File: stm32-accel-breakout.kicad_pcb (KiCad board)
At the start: 2 copper layers, 43.1 x 38 mm, 42 parts, among them J1 USB_C_Receptacle_USB2.0, J2 JST-PH-01x05, J3 Conn_01x03, J5 Conn_01x04, U1 STM32F103C8Tx, U2 AP2112K-3.3, U3 ADXL335, Y1 Crystal_GND24

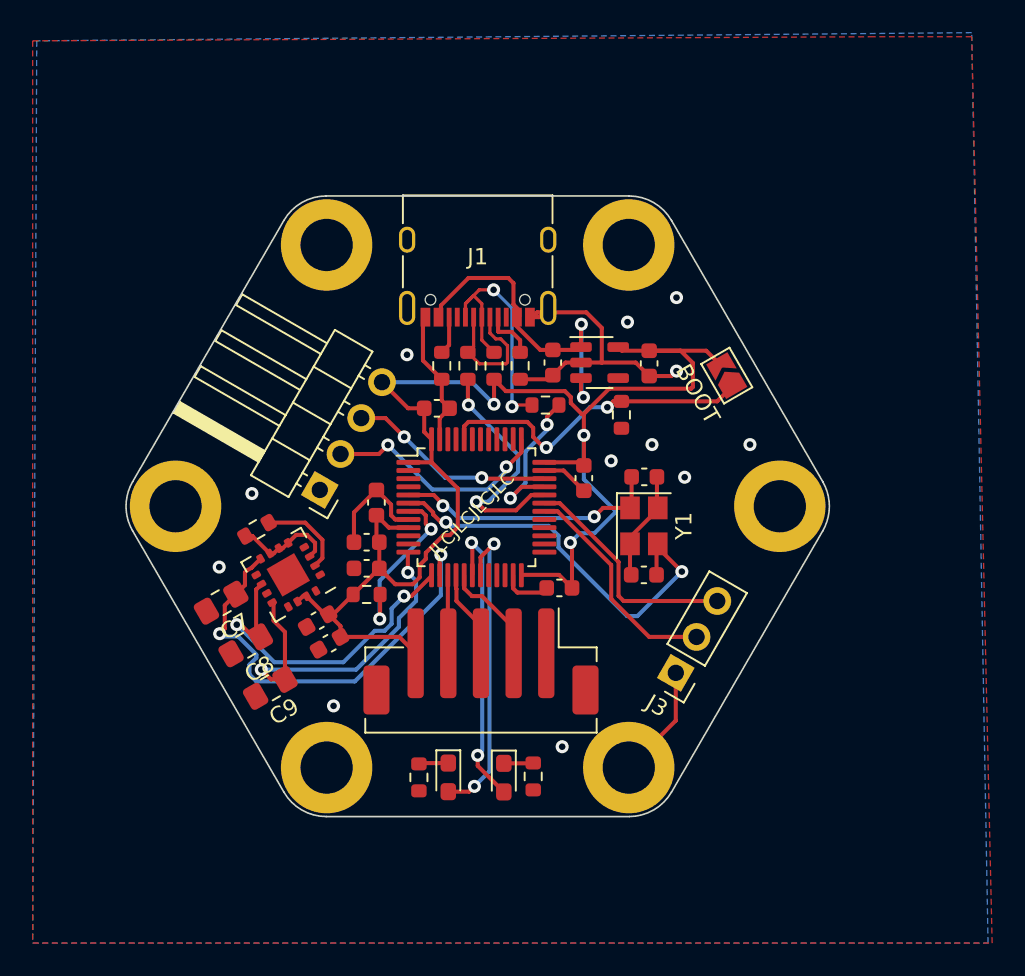
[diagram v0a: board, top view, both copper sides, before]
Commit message: changed programming header to tag connect
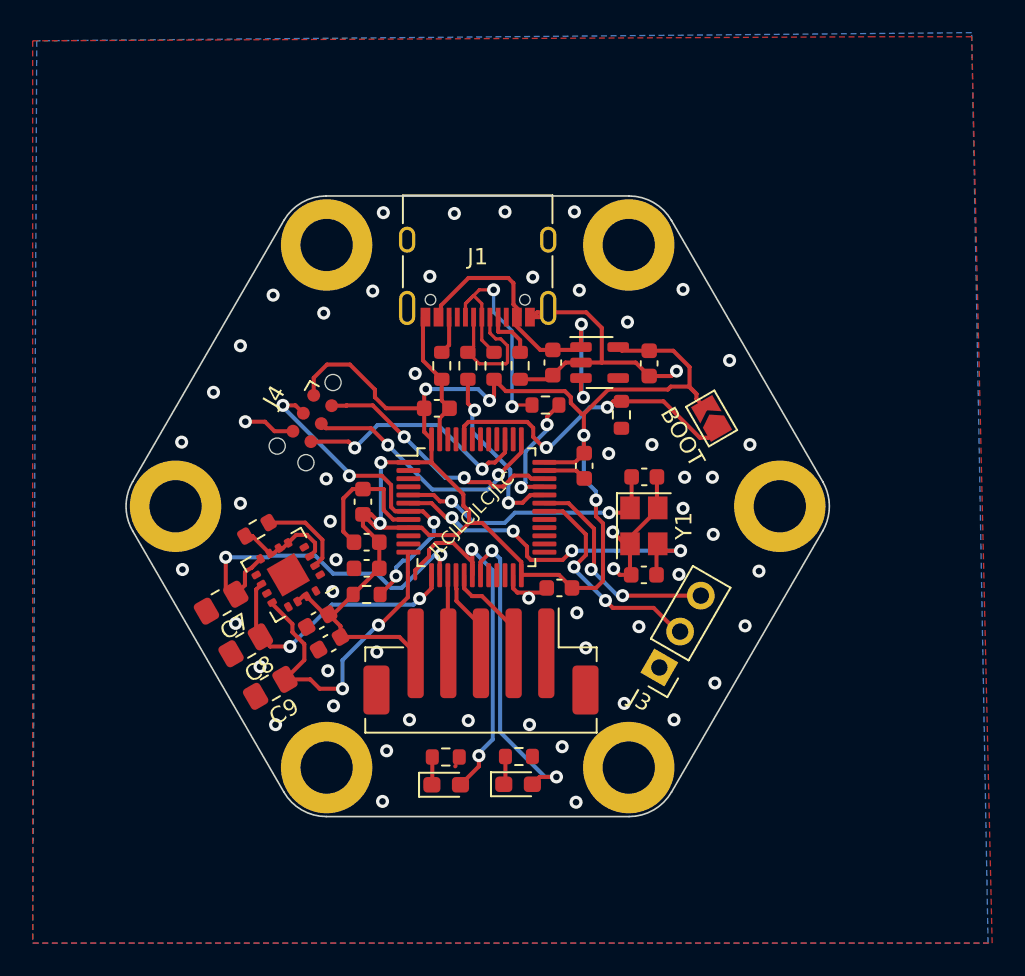
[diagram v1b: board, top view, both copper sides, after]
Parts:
- removed J5: Conn_01x04, Connector_PinHeader_2.54mm:PinHeader_1x04_P2.54mm_Horizontal
- added J4: Conn_ARM_SWD_TagConnect_TC2030-NL, Connector:Tag-Connect_TC2030-IDC-NL_2x03_P1.27mm_Vertical, F.Cu at (139.7, 94.9)
- R10, R9: value 22 -> 1k
- moved R10 6.25 mm to (152.3, 115.6), turned to 180 degrees
- moved R9 5.48 mm to (147.9, 115.6), turned to 180 degrees
- moved D2 4.29 mm to (152.3, 117.3), turned to 0 degrees
- moved D1 3.56 mm to (147.9, 117.3), turned to 0 degrees
- moved JP1 2.78 mm to (164.2, 94.9)
- moved J3 1.06 mm to (160.9, 110.2)
- moved C5 0.83 mm to (142.8, 100.0)
- moved C3 0.75 mm to (156.3, 97.8)
- renumbered He to H3
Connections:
- net Net-(U1-NRST) renamed RST
- U1 pad 39: unconnected-(U1-PB3-Pad39) -> SWO
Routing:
- net SWO: track 0.00 -> 15.0 mm, vias 0 -> 2
- net RST: track 10.5 -> 20.6 mm, vias 2 -> 4
- net +3.3V: track 94.3 -> 104.4 mm, vias 3 -> 6
- net ADXL_Z1_{out}: track 27.7 -> 21.7 mm
- net Net-(D1-A): track 18.3 -> 23.6 mm
- net ADXL_Y1_{out}: track 20.9 -> 16.5 mm
- net Net-(U1-PD1): track 25.5 -> 22.3 mm, vias 2 -> 4
- net Net-(U1-PA11): track 15.0 -> 12.0 mm
- net SWDIO: track 12.8 -> 15.5 mm
- net Net-(U1-PA12): track 9.30 -> 7.45 mm
- net SWCLK: track 14.3 -> 15.8 mm
- net ADXL_X1_{out}: track 21.5 -> 20.1 mm
- net RX1: track 14.3 -> 13.6 mm, vias 0 -> 2
- net GND: track 60.3 -> 60.8 mm, vias 12 -> 57
- net TX1: track 13.7 -> 13.6 mm, vias 0 -> 2

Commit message: changed connector for breakout accelerometer to jst-sh
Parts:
- J2: value JST-PH-01x05 -> JST-SH-01x05; footprint Connector_JST:JST_PH_B5B-PH-SM4-TB_1x05-1MP_P2.00mm_Vertical -> Connector_JST:JST_SH_BM05B-SRSS-TB_1x05-1MP_P1.00mm_Vertical
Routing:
- net Net-(D1-A): track 23.6 -> 17.4 mm
- net GND: track 60.8 -> 64.0 mm
- net ADXL_Z2_{out}: track 6.39 -> 4.79 mm
- net +3.3V: track 104.4 -> 105.9 mm
- net ADXL_Y2_{out}: track 5.41 -> 4.59 mm
- net RX1: track 13.6 -> 14.4 mm

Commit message: final edits before sending PCBs for fabrication. 10 boards ordered from JLCPCB
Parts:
- H1, H2, H3, H4, H5, H6: footprint MountingHole:MountingHole_3.2mm_M3_DIN965_Pad -> MountingHole:MountingHole_2.7mm_M2.5_DIN965_Pad
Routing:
- net GND: track 64.0 -> 65.1 mm
